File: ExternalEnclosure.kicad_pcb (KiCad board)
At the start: 2 copper layers, 81.7 x 34.6 mm, 81 parts, among them J1 Molex 0472861001, J2 Molex 0472861001, J3 Molex 0472861001, J4 Molex 0472861001, U1 XC6206P332MR-G, U2 SY6280AAC, U3 GL852G-OHY60_C7501404, U4 CH32V003F4U6, U5 SY6280AAC, X1 12MHz

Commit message: Add back side SMT header for power profiling
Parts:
- added J5: Power Profiling, Connector_PinHeader_2.54mm:PinHeader_2x03_P2.54mm_Vertical_SMD, B.Cu at (133.1, 111.3)
- added NT1: NetTie_2, NetTie:NetTie-2_SMD_Pad0.5mm, B.Cu at (133.2, 111.2)
- added NT2: NetTie_2, NetTie:NetTie-2_SMD_Pad0.5mm, B.Cu at (133.1, 108.7)
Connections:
- C17 pad 1: +5VP -> Net-(D5-VBUS)
- C18 pad 1: +3.3VP -> Net-(D6-VBUS)
- C19 pad 1: +5VP -> Net-(D5-VBUS)
- C20 pad 1: +3.3VP -> Net-(D6-VBUS)
- D5 pad 5: +5VP -> Net-(D5-VBUS)
- D6 pad 5: +3.3VP -> Net-(D6-VBUS)
- J4 pad 1: +3.3VP -> Net-(D6-VBUS)
- J4 pad 4: +5VP -> Net-(D5-VBUS)
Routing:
- net Net-(D6-VBUS): track 0.00 -> 39.9 mm, vias 0 -> 1
- net Net-(D5-VBUS): track 0.00 -> 31.9 mm, vias 0 -> 1
- net +5VP: track 95.7 -> 75.6 mm, vias 3 -> 2
- net GND: track 372.8 -> 379.5 mm, vias 55 -> 59
- net +3.3VP: track 122.1 -> 125.1 mm, vias 4 -> 5

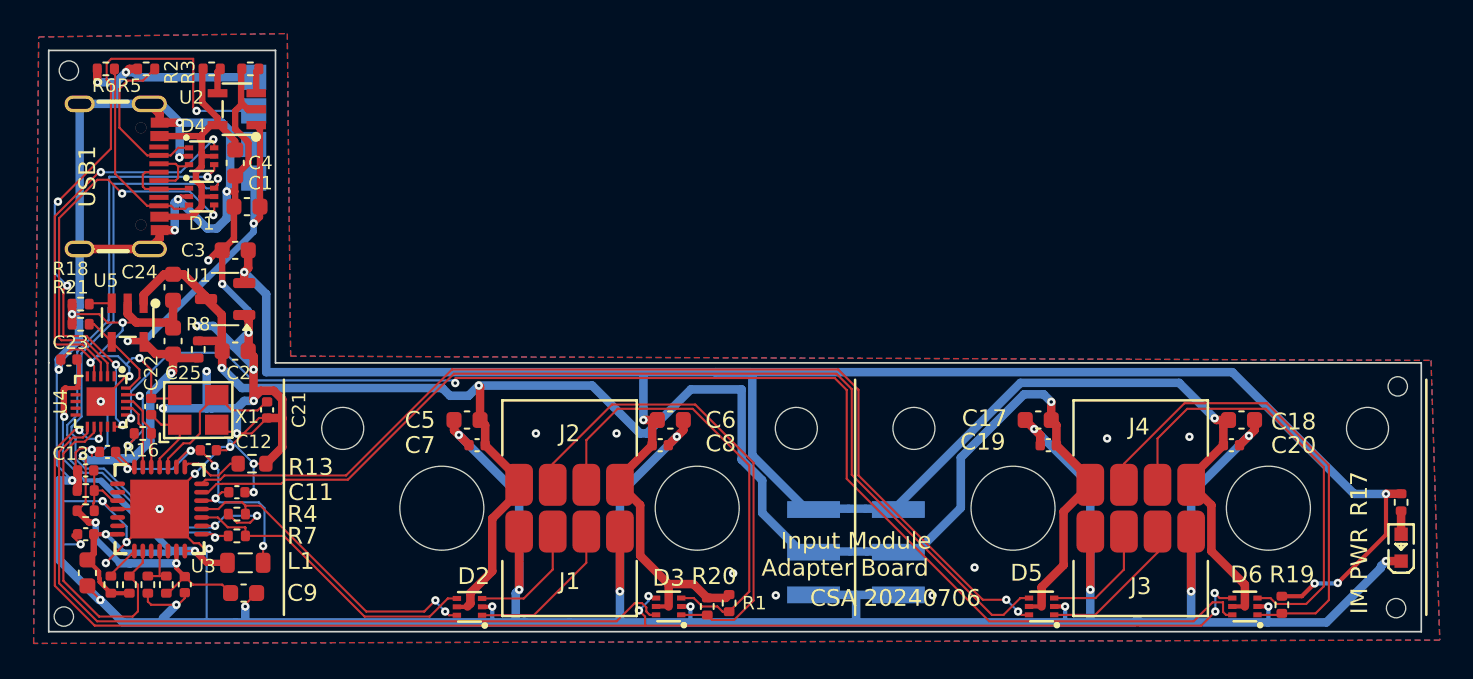
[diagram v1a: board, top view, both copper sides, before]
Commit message: Tweak bottom clearances, change to slot for magnets on PCB
The bottom clearances weren't quite right around the pogo pin area, and
although my own PCBs made appropriate contact with the pogo pins, the
official Framework LED Matrix input module was about 1mm (!) short of
proper contact with the pins/magnet.  A couple of things:
* My "5mm diameter x 2mm thick" magnets were actually only 1.6mm thick
* It appears that we need an extra 0.5mm clearance between the "thick
  component" area and the pogo pin area.  The nominal clearance here is
  0.4mm but the Framework-supplied module was contacting here.
* The pogo pin plane should have been measured from the PCB bottom,
  which is 0.5mm above the "spacer bottom" level.

That last adjustment also moved the USB connector up by proxy, so we
needed to add a little bit of a bump over it to ensure a reasonable
minimum width for the shell here.  It's possible we'll remove the top
entirely here and fold this into the lid, but that complicates printing
the lid on a FDM 3d printer because the lid top is no longer planer. So
leave it as-is with a bit of a bump for now.

I also adjusted the cutout in the case so that it would accomodate the
original PCB design as well as the new one, since I have 5 perfectly
functional v1 boards.

The magnets also weren't very grabby.  This is party because they were
too far away from the steel (see above) but I decided to beef this up as
well.  Looking at the FW16 midplate it appears that a pair of opposite
polarity magnets is used.  Switch to an oval slot on the PCB so that we
can use a pair of magnets in our version as well.
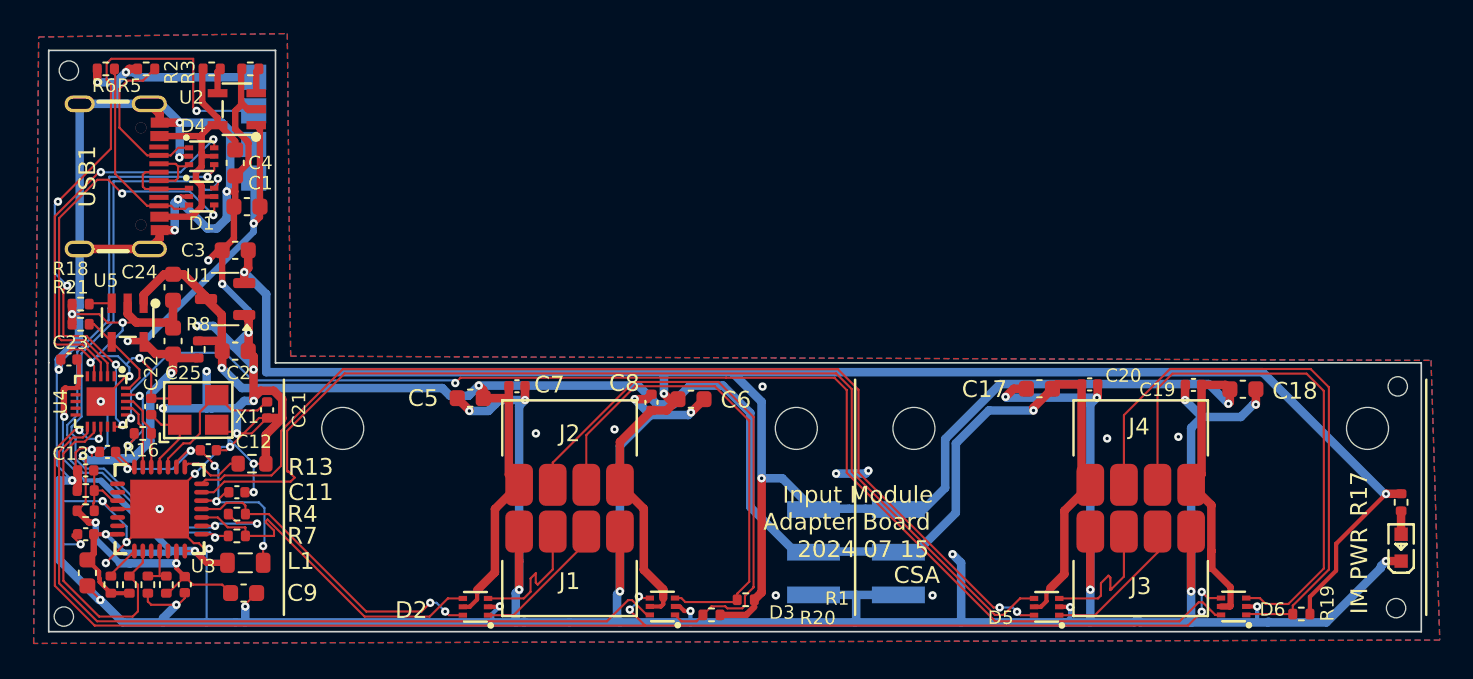
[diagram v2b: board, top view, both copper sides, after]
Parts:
- H1, H10, H2, H9: footprint ExternalMount:MountingHole_5mm_no_keepout -> ExternalMount:MountingHole_5mm_slot_no_keepout
- moved C19 4.38 mm to (147.0, 101.3), turned to 0 degrees
- moved C20 4.24 mm to (153.1, 101.3), turned to 180 degrees
- moved C7 4.24 mm to (112.9, 101.4), turned to 0 degrees
- moved C8 2.60 mm to (120.9, 102.3), turned to 90 degrees
- moved C17 1.86 mm to (144.0, 101.5)
- moved C18 1.83 mm to (156.1, 101.6)
- moved C6 1.75 mm to (123.2, 102.2)
- moved C5 1.31 mm to (110.1, 102.1)
- moved R19 1.28 mm to (159.6, 115.0), turned to 180 degrees
- moved R1 1.01 mm to (126.5, 114.1), turned to 180 degrees
- moved D6 0.67 mm to (155.5, 114.5)
- moved R20 0.56 mm to (124.5, 115.0), turned to 180 degrees
- moved D3 0.37 mm to (121.5, 114.5)
- moved D2 0.36 mm to (110.4, 114.5)
- moved D5 0.30 mm to (144.4, 114.5)
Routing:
- net GND: track 379.5 -> 407.0 mm, vias 59 -> 65
- net /~{SLEEP2_UNP}: track 26.5 -> 32.6 mm
- net /BOARD_ID2_UNP: track 29.1 -> 35.2 mm
- net Net-(D6-VBUS): track 39.9 -> 44.6 mm
- net +3.3VP: track 125.1 -> 129.2 mm, vias 5 -> 4
- net /BOARD_ID1_UNP: track 29.2 -> 32.4 mm
- net Net-(D5-VBUS): track 31.9 -> 34.5 mm
- net /~{SLEEP1_UNP}: track 26.9 -> 29.5 mm
- net /USB_DM2: track 61.5 -> 64.0 mm
- net /USB_DM1: track 18.4 -> 20.7 mm
- net Net-(J3-Pin_2): track 7.12 -> 8.65 mm
- net /USB_DP2: track 61.1 -> 62.5 mm
- net /BOARD_ID2: track 79.7 -> 78.4 mm
- net Net-(J1-Pin_3): track 9.36 -> 8.30 mm
- net Net-(J1-Pin_2): track 7.18 -> 8.17 mm
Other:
- board text added: "2024 07 15"
- board text added: "CSA"
- board text removed: "CSA 20240706"
